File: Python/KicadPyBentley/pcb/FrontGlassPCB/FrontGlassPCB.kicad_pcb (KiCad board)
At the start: 4 copper layers, 177.3 x 82.5 mm, 3 parts

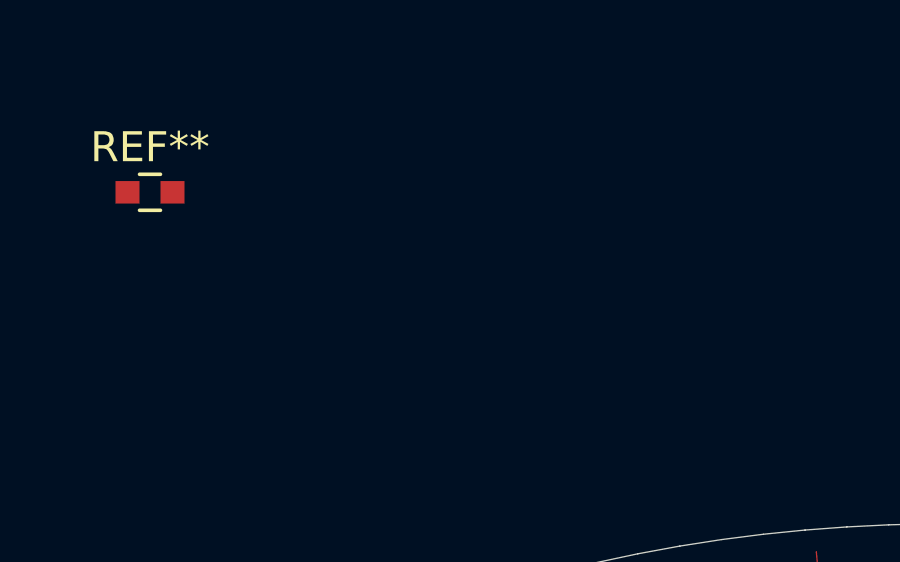
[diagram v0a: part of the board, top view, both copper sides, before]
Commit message: changed net management
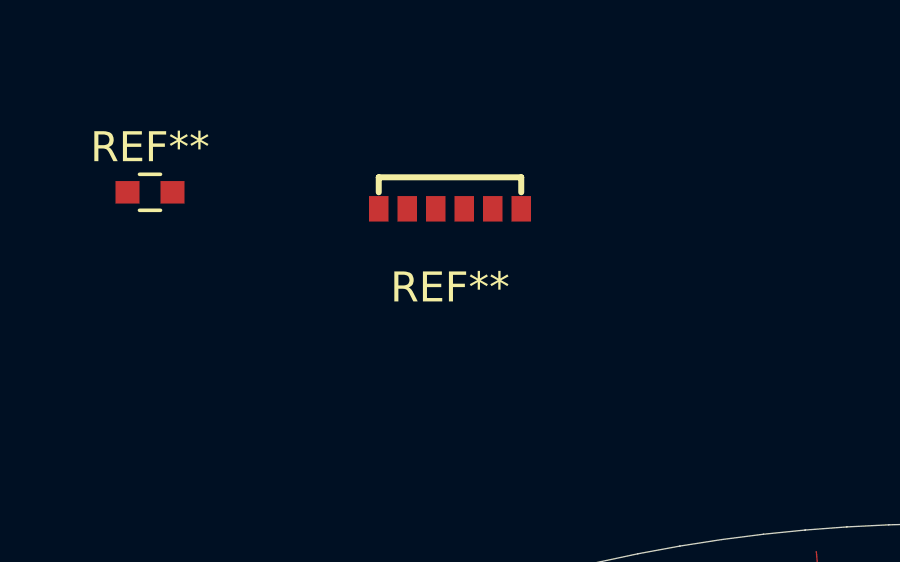
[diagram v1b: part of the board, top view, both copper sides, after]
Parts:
- added REF**: CL-Z891, CL-Z891, B.Cu at (30.0, 0.00)
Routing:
- net (no net): track 0.00 -> 10402.9 mm, vias 0 -> 1104
- net VI: track 6037.4 -> 0.00 mm
- net VO: track 4365.4 -> 0.00 mm, vias 1104 -> 0

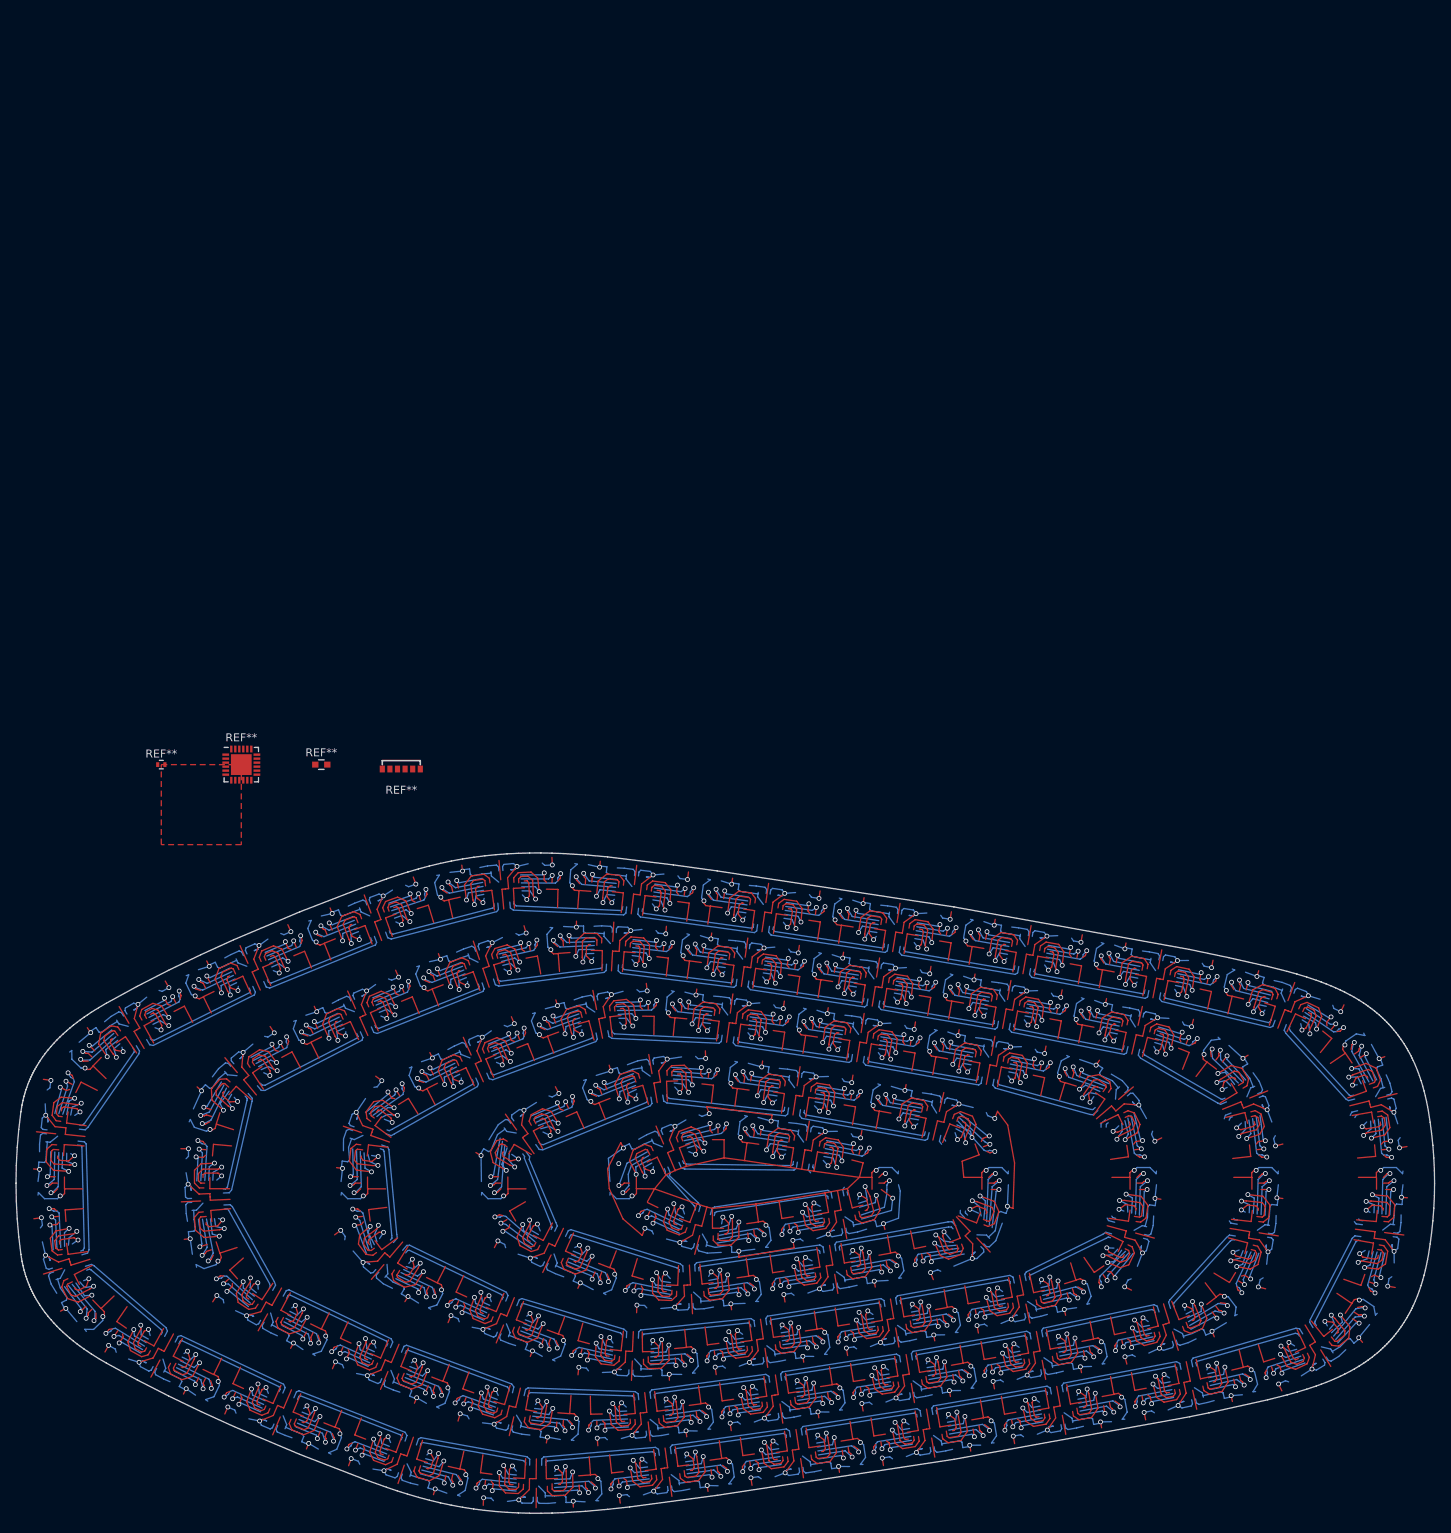
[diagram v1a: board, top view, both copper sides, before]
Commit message: added csv footprint reader
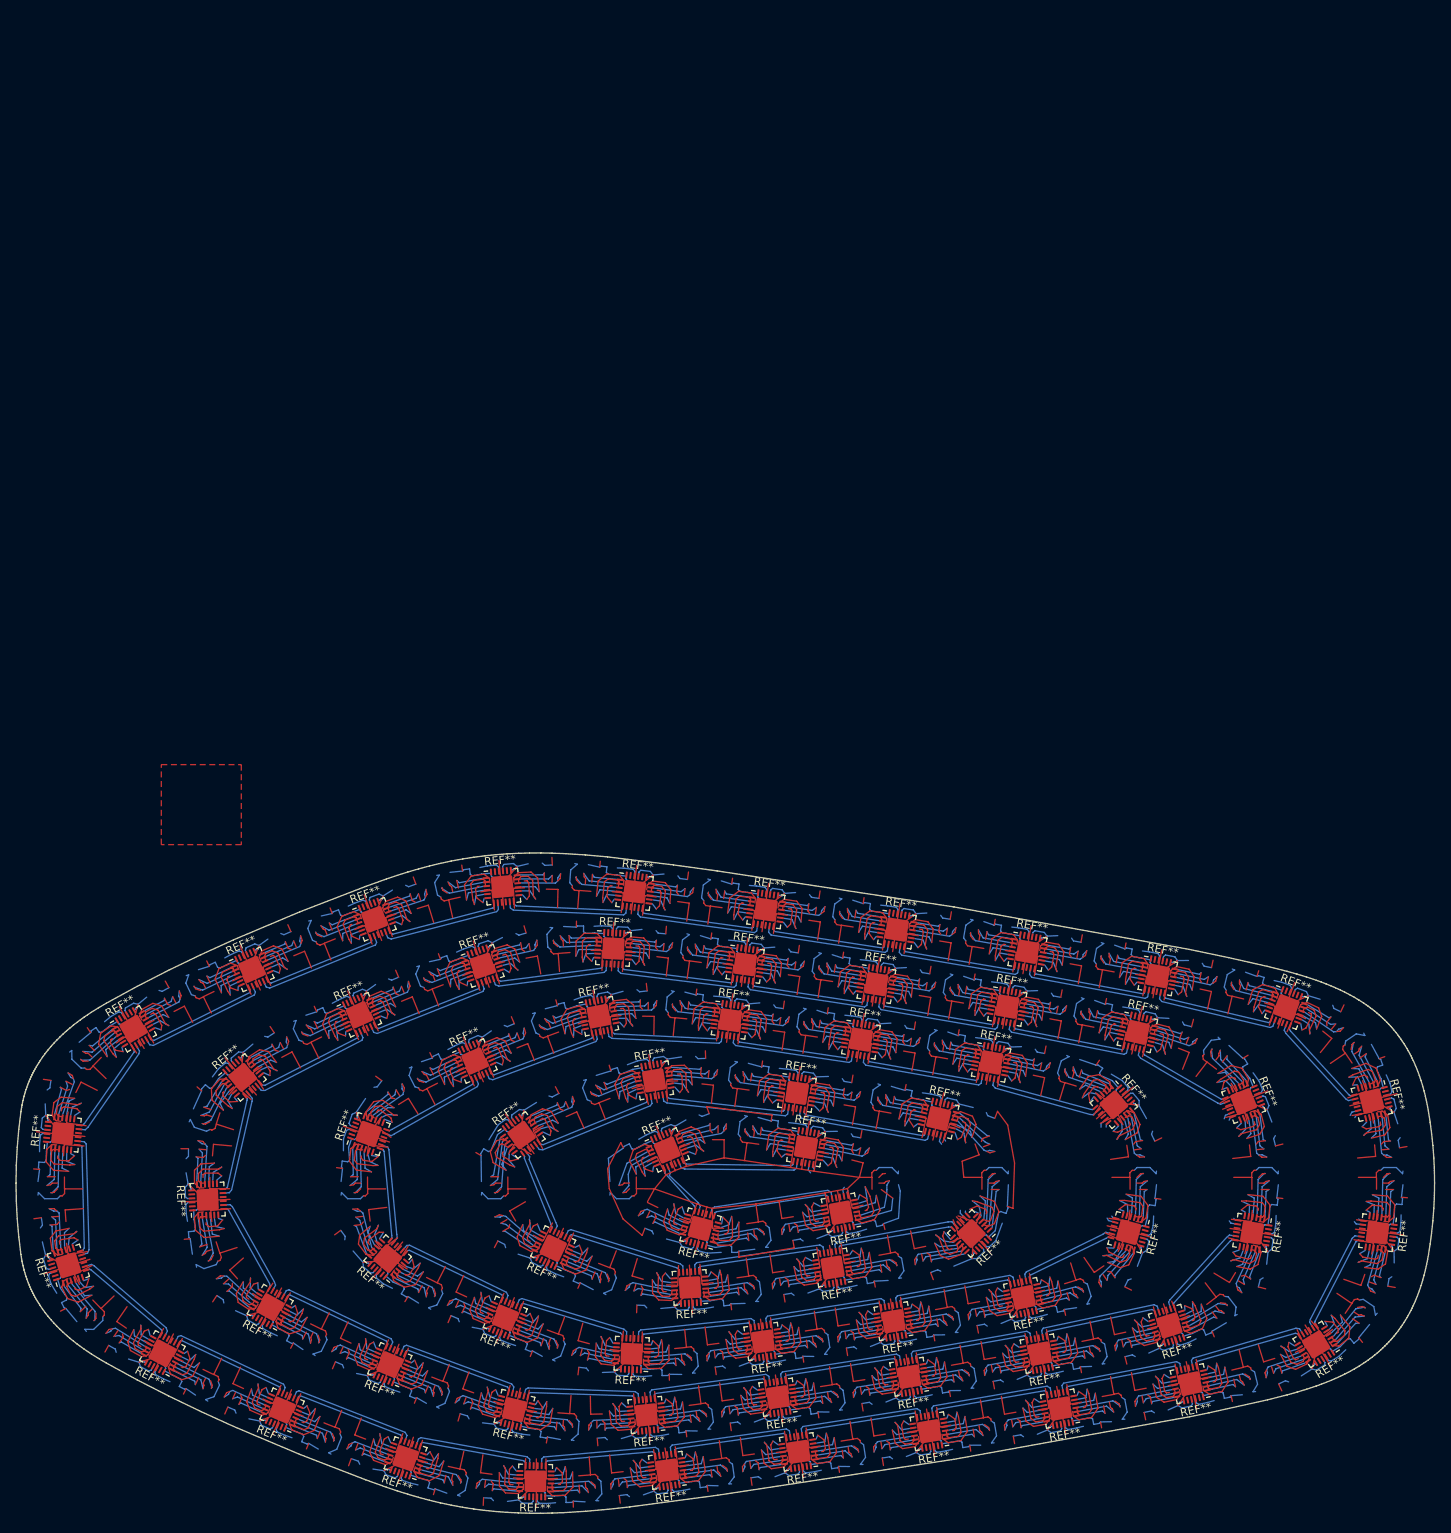
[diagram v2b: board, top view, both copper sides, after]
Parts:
- removed the REF** at (0.00, 0.00)
- removed the REF** at (10.0, 0.00)
- removed the REF** at (20.0, 0.00)
- removed the REF** at (30.0, 0.00)
- added REF**: Texas_RGE0024H_EP2.7x2.7mm, Texas_RGE0024H_EP2.7x2.7mm, B.Cu at (101.3, 58.6)
- added REF**: Texas_RGE0024H_EP2.7x2.7mm, Texas_RGE0024H_EP2.7x2.7mm, B.Cu at (107.8, 66.6)
- added REF**: Texas_RGE0024H_EP2.7x2.7mm, Texas_RGE0024H_EP2.7x2.7mm, B.Cu at (91.5, 69.6)
- added REF**: Texas_RGE0024H_EP2.7x2.7mm, Texas_RGE0024H_EP2.7x2.7mm, B.Cu at (75.2, 72.1)
- added REF**: Texas_RGE0024H_EP2.7x2.7mm, Texas_RGE0024H_EP2.7x2.7mm, B.Cu at (58.8, 73.7)
- added REF**: Texas_RGE0024H_EP2.7x2.7mm, Texas_RGE0024H_EP2.7x2.7mm, B.Cu at (43.0, 69.2)
- added REF**: Texas_RGE0024H_EP2.7x2.7mm, Texas_RGE0024H_EP2.7x2.7mm, B.Cu at (28.3, 61.8)
- added REF**: Texas_RGE0024H_EP2.7x2.7mm, Texas_RGE0024H_EP2.7x2.7mm, B.Cu at (25.9, 46.2)
- added REF**: Texas_RGE0024H_EP2.7x2.7mm, Texas_RGE0024H_EP2.7x2.7mm, B.Cu at (39.2, 37.0)
- added REF**: Texas_RGE0024H_EP2.7x2.7mm, Texas_RGE0024H_EP2.7x2.7mm, B.Cu at (54.7, 31.4)
- added REF**: Texas_RGE0024H_EP2.7x2.7mm, Texas_RGE0024H_EP2.7x2.7mm, B.Cu at (71.1, 31.9)
- added REF**: Texas_RGE0024H_EP2.7x2.7mm, Texas_RGE0024H_EP2.7x2.7mm, B.Cu at (83.9, 62.9)
- added REF**: Texas_RGE0024H_EP2.7x2.7mm, Texas_RGE0024H_EP2.7x2.7mm, B.Cu at (87.5, 34.4)
- added REF**: Texas_RGE0024H_EP2.7x2.7mm, Texas_RGE0024H_EP2.7x2.7mm, B.Cu at (103.7, 37.2)
- added REF**: Texas_RGE0024H_EP2.7x2.7mm, Texas_RGE0024H_EP2.7x2.7mm, B.Cu at (119.1, 42.5)
- added REF**: Texas_RGE0024H_EP2.7x2.7mm, Texas_RGE0024H_EP2.7x2.7mm, B.Cu at (136.3, 58.5)
- added REF**: Texas_RGE0024H_EP2.7x2.7mm, Texas_RGE0024H_EP2.7x2.7mm, B.Cu at (126.0, 70.1)
- added REF**: Texas_RGE0024H_EP2.7x2.7mm, Texas_RGE0024H_EP2.7x2.7mm, B.Cu at (109.8, 73.6)
- added REF**: Texas_RGE0024H_EP2.7x2.7mm, Texas_RGE0024H_EP2.7x2.7mm, B.Cu at (93.5, 76.5)
- added REF**: Texas_RGE0024H_EP2.7x2.7mm, Texas_RGE0024H_EP2.7x2.7mm, B.Cu at (77.1, 79.1)
- added REF**: Texas_RGE0024H_EP2.7x2.7mm, Texas_RGE0024H_EP2.7x2.7mm, B.Cu at (60.6, 81.3)
- added REF**: Texas_RGE0024H_EP2.7x2.7mm, Texas_RGE0024H_EP2.7x2.7mm, B.Cu at (44.1, 80.6)
- added REF**: Texas_RGE0024H_EP2.7x2.7mm, Texas_RGE0024H_EP2.7x2.7mm, B.Cu at (66.1, 65.4)
- added REF**: Texas_RGE0024H_EP2.7x2.7mm, Texas_RGE0024H_EP2.7x2.7mm, B.Cu at (28.6, 75.0)
- added REF**: Texas_RGE0024H_EP2.7x2.7mm, Texas_RGE0024H_EP2.7x2.7mm, B.Cu at (13.6, 67.8)
- added REF**: Texas_RGE0024H_EP2.7x2.7mm, Texas_RGE0024H_EP2.7x2.7mm, B.Cu at (5.79, 54.4)
- added REF**: Texas_RGE0024H_EP2.7x2.7mm, Texas_RGE0024H_EP2.7x2.7mm, B.Cu at (10.2, 39.1)
- added REF**: Texas_RGE0024H_EP2.7x2.7mm, Texas_RGE0024H_EP2.7x2.7mm, B.Cu at (24.8, 31.3)
- added REF**: Texas_RGE0024H_EP2.7x2.7mm, Texas_RGE0024H_EP2.7x2.7mm, B.Cu at (40.2, 25.1)
- added REF**: Texas_RGE0024H_EP2.7x2.7mm, Texas_RGE0024H_EP2.7x2.7mm, B.Cu at (56.5, 23.0)
- added REF**: Texas_RGE0024H_EP2.7x2.7mm, Texas_RGE0024H_EP2.7x2.7mm, B.Cu at (73.0, 25.0)
- added REF**: Texas_RGE0024H_EP2.7x2.7mm, Texas_RGE0024H_EP2.7x2.7mm, B.Cu at (89.4, 27.4)
- added REF**: Texas_RGE0024H_EP2.7x2.7mm, Texas_RGE0024H_EP2.7x2.7mm, B.Cu at (105.7, 30.2)
- added REF**: Texas_RGE0024H_EP2.7x2.7mm, Texas_RGE0024H_EP2.7x2.7mm, B.Cu at (49.0, 60.5)
- added REF**: Texas_RGE0024H_EP2.7x2.7mm, Texas_RGE0024H_EP2.7x2.7mm, B.Cu at (122.0, 33.5)
- added REF**: Texas_RGE0024H_EP2.7x2.7mm, Texas_RGE0024H_EP2.7x2.7mm, B.Cu at (135.3, 42.1)
- added REF**: Texas_RGE0024H_EP2.7x2.7mm, Texas_RGE0024H_EP2.7x2.7mm, B.Cu at (152.0, 58.5)
- added REF**: Texas_RGE0024H_EP2.7x2.7mm, Texas_RGE0024H_EP2.7x2.7mm, B.Cu at (144.4, 72.5)
- added REF**: Texas_RGE0024H_EP2.7x2.7mm, Texas_RGE0024H_EP2.7x2.7mm, B.Cu at (128.6, 77.4)
- added REF**: Texas_RGE0024H_EP2.7x2.7mm, Texas_RGE0024H_EP2.7x2.7mm, B.Cu at (112.3, 80.5)
- added REF**: Texas_RGE0024H_EP2.7x2.7mm, Texas_RGE0024H_EP2.7x2.7mm, B.Cu at (96.0, 83.3)
- added REF**: Texas_RGE0024H_EP2.7x2.7mm, Texas_RGE0024H_EP2.7x2.7mm, B.Cu at (79.7, 85.9)
- added REF**: Texas_RGE0024H_EP2.7x2.7mm, Texas_RGE0024H_EP2.7x2.7mm, B.Cu at (63.3, 88.2)
- added REF**: Texas_RGE0024H_EP2.7x2.7mm, Texas_RGE0024H_EP2.7x2.7mm, B.Cu at (46.8, 89.6)
- added REF**: Texas_RGE0024H_EP2.7x2.7mm, Texas_RGE0024H_EP2.7x2.7mm, B.Cu at (45.0, 46.3)
- added REF**: Texas_RGE0024H_EP2.7x2.7mm, Texas_RGE0024H_EP2.7x2.7mm, B.Cu at (30.5, 86.7)
- added REF**: Texas_RGE0024H_EP2.7x2.7mm, Texas_RGE0024H_EP2.7x2.7mm, B.Cu at (15.1, 80.7)
- added REF**: Texas_RGE0024H_EP2.7x2.7mm, Texas_RGE0024H_EP2.7x2.7mm, B.Cu at (0.14, 73.6)
- added REF**: Texas_RGE0024H_EP2.7x2.7mm, Texas_RGE0024H_EP2.7x2.7mm, B.Cu at (-11.6, 62.6)
- added REF**: Texas_RGE0024H_EP2.7x2.7mm, Texas_RGE0024H_EP2.7x2.7mm, B.Cu at (-12.3, 46.1)
- added REF**: Texas_RGE0024H_EP2.7x2.7mm, Texas_RGE0024H_EP2.7x2.7mm, B.Cu at (-3.49, 33.0)
- added REF**: Texas_RGE0024H_EP2.7x2.7mm, Texas_RGE0024H_EP2.7x2.7mm, B.Cu at (11.3, 25.6)
- added REF**: Texas_RGE0024H_EP2.7x2.7mm, Texas_RGE0024H_EP2.7x2.7mm, B.Cu at (26.6, 19.3)
- added REF**: Texas_RGE0024H_EP2.7x2.7mm, Texas_RGE0024H_EP2.7x2.7mm, B.Cu at (42.6, 15.3)
- added REF**: Texas_RGE0024H_EP2.7x2.7mm, Texas_RGE0024H_EP2.7x2.7mm, B.Cu at (59.2, 15.9)
- added REF**: Texas_RGE0024H_EP2.7x2.7mm, Texas_RGE0024H_EP2.7x2.7mm, B.Cu at (61.6, 39.5)
- added REF**: Texas_RGE0024H_EP2.7x2.7mm, Texas_RGE0024H_EP2.7x2.7mm, B.Cu at (75.6, 18.1)
- added REF**: Texas_RGE0024H_EP2.7x2.7mm, Texas_RGE0024H_EP2.7x2.7mm, B.Cu at (91.9, 20.6)
- added REF**: Texas_RGE0024H_EP2.7x2.7mm, Texas_RGE0024H_EP2.7x2.7mm, B.Cu at (108.3, 23.4)
- added REF**: Texas_RGE0024H_EP2.7x2.7mm, Texas_RGE0024H_EP2.7x2.7mm, B.Cu at (124.6, 26.4)
- added REF**: Texas_RGE0024H_EP2.7x2.7mm, Texas_RGE0024H_EP2.7x2.7mm, B.Cu at (140.6, 30.4)
- added REF**: Texas_RGE0024H_EP2.7x2.7mm, Texas_RGE0024H_EP2.7x2.7mm, B.Cu at (151.3, 42.0)
- added REF**: Texas_RGE0024H_EP2.7x2.7mm, Texas_RGE0024H_EP2.7x2.7mm, B.Cu at (85.0, 56.0)
- added REF**: Texas_RGE0024H_EP2.7x2.7mm, Texas_RGE0024H_EP2.7x2.7mm, B.Cu at (67.4, 58.0)
- added REF**: Texas_RGE0024H_EP2.7x2.7mm, Texas_RGE0024H_EP2.7x2.7mm, B.Cu at (63.2, 48.2)
- added REF**: Texas_RGE0024H_EP2.7x2.7mm, Texas_RGE0024H_EP2.7x2.7mm, B.Cu at (80.6, 47.8)
- added REF**: Texas_RGE0024H_EP2.7x2.7mm, Texas_RGE0024H_EP2.7x2.7mm, B.Cu at (79.5, 41.0)
- added REF**: Texas_RGE0024H_EP2.7x2.7mm, Texas_RGE0024H_EP2.7x2.7mm, B.Cu at (97.2, 44.2)
- added REF**: Texas_RGE0024H_EP2.7x2.7mm, Texas_RGE0024H_EP2.7x2.7mm, B.Cu at (120.9, 58.4)
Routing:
- net (no net): vias 1104 -> 0

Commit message: added front/back functionality to footprints
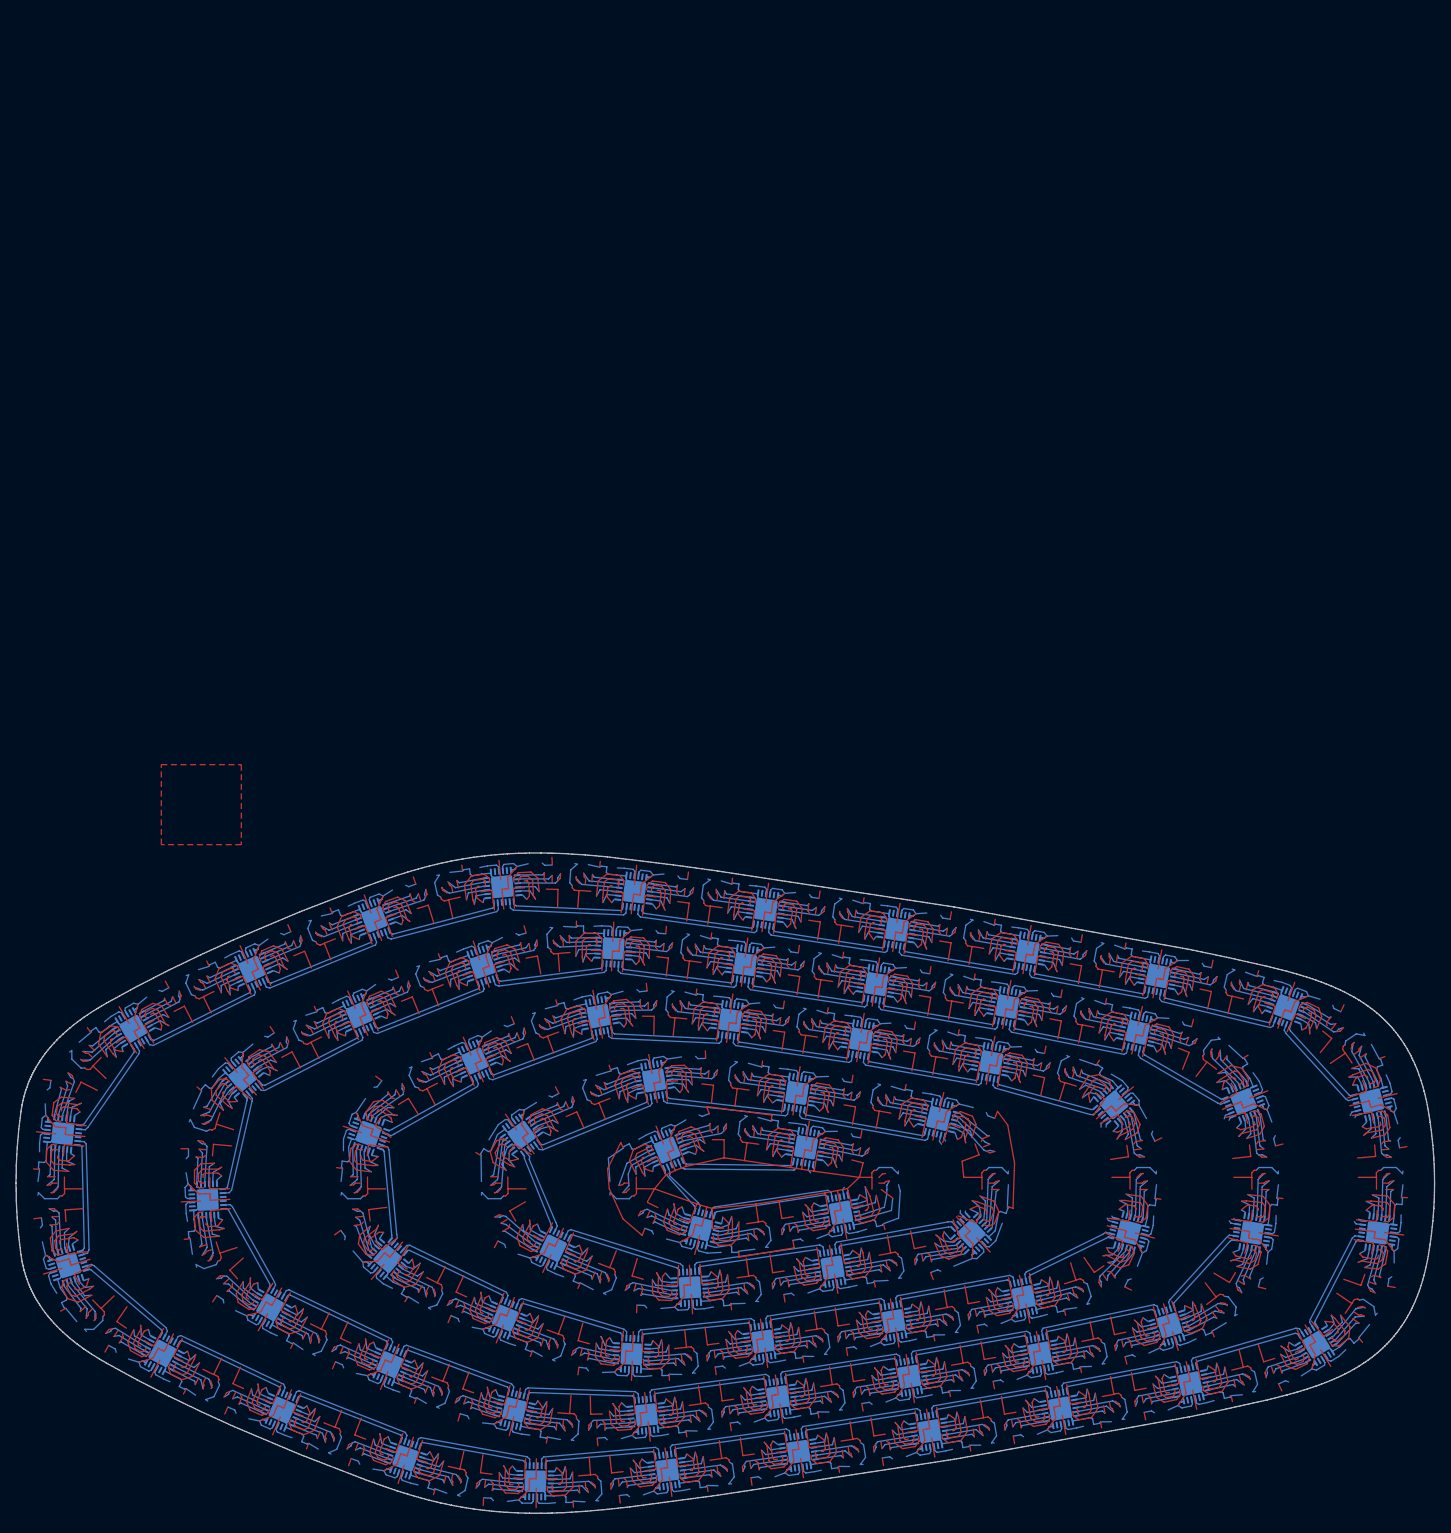
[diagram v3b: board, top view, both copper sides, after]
